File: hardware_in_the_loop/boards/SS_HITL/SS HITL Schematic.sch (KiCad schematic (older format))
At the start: 24 parts, among them J1 CONN_02X03, U2 ATMEGA16M1, Y1 Crystal_SMD

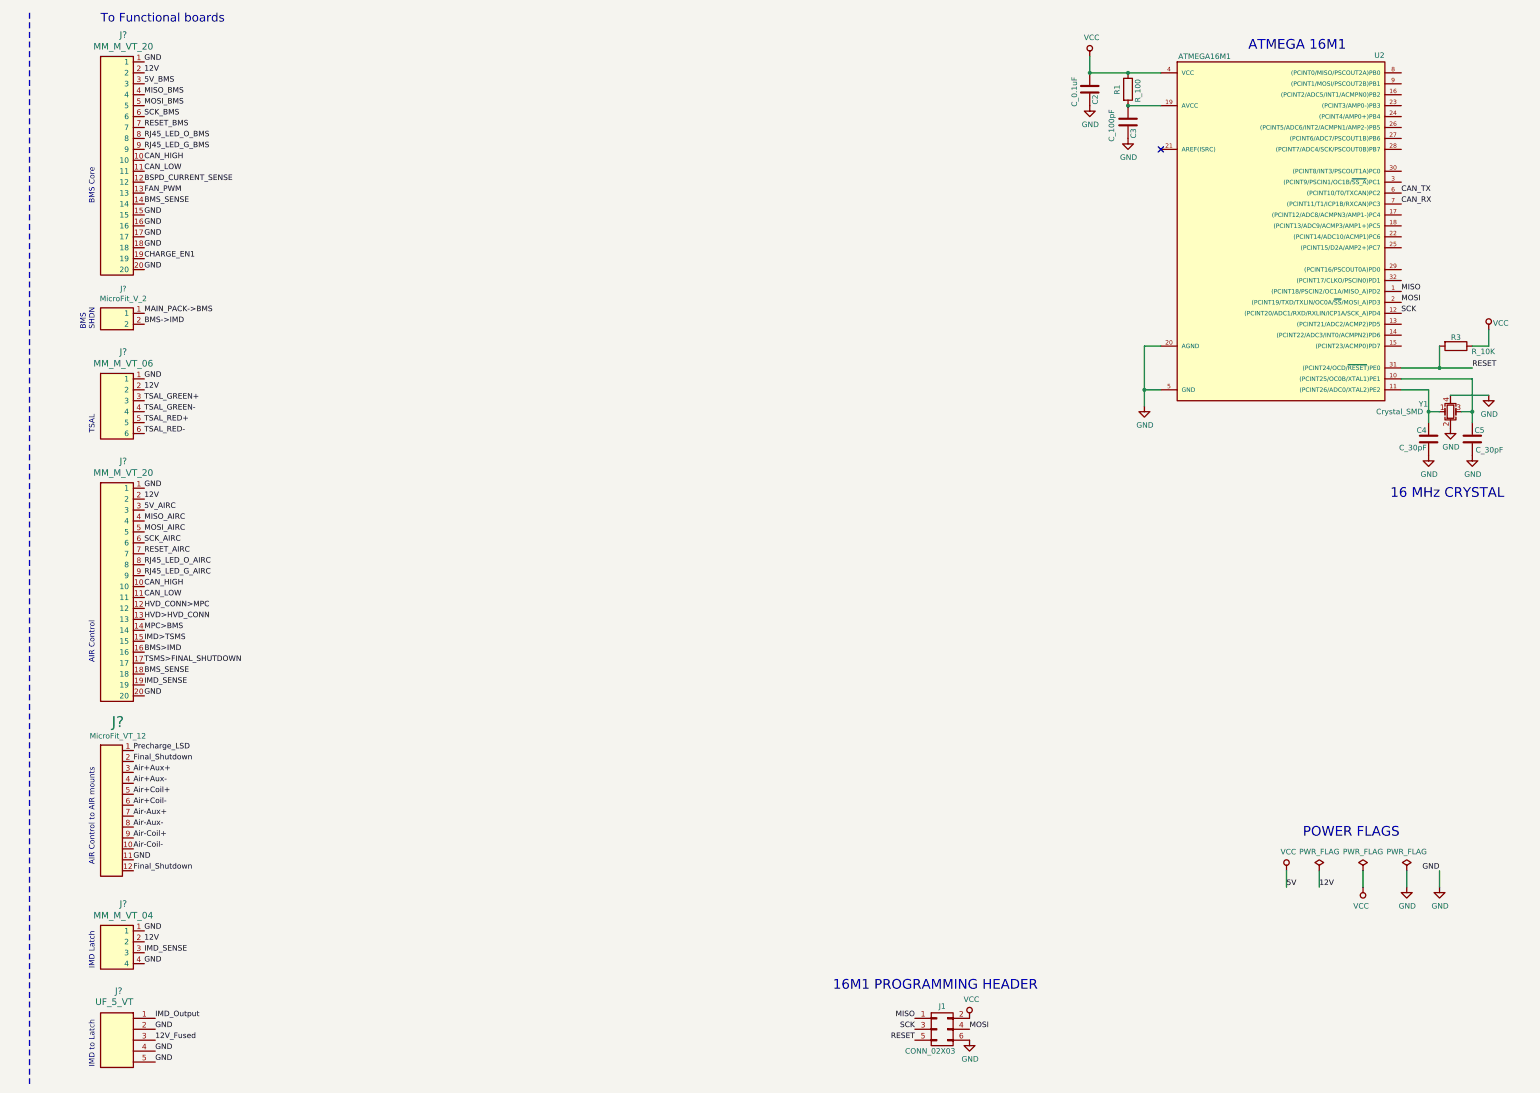
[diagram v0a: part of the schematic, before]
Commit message: Finalized pins on connectors, started to block out mux/demux.
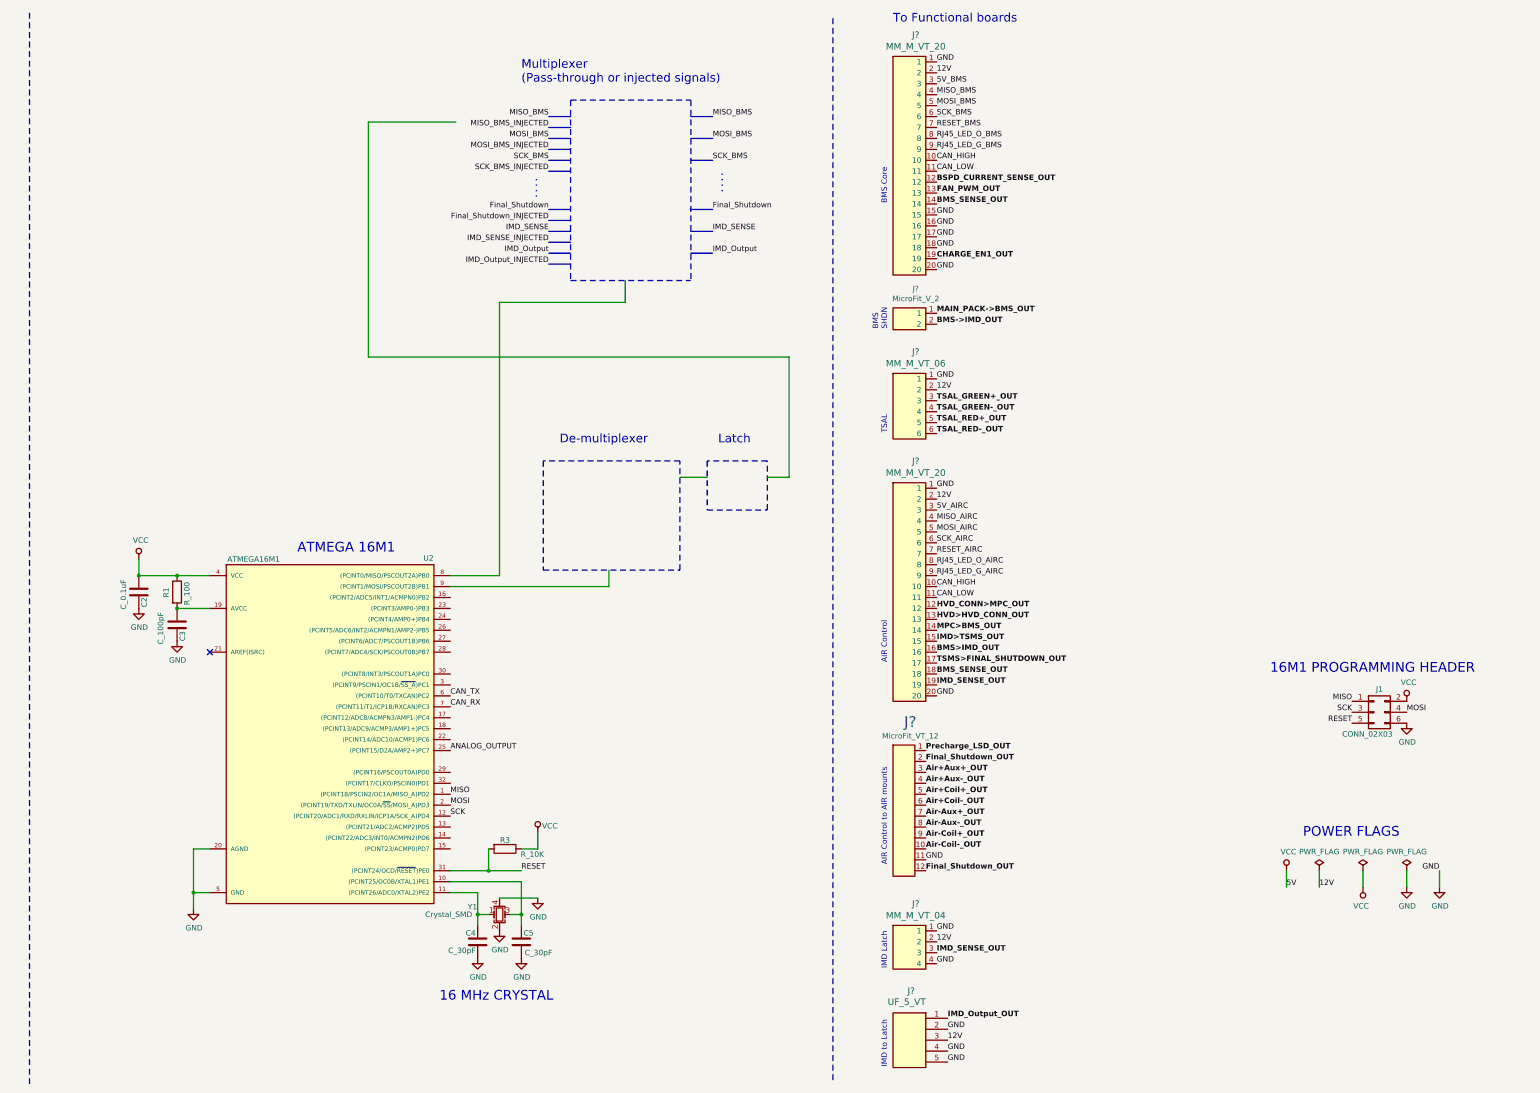
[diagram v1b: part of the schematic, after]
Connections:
- net labels added: ANALOG_OUTPUT, Air+Aux+_OUT, Air+Aux-_OUT, Air+Coil+_OUT, Air+Coil-_OUT, Air-Aux+_OUT, Air-Aux-_OUT, Air-Coil+_OUT, Air-Coil-_OUT, BMS->IMD_OUT, BMS>IMD_OUT, BMS_SENSE_OUT, BSPD_CURRENT_SENSE_OUT, CHARGE_EN1_OUT, FAN_PWM_OUT, Final_Shutdown_INJECTED, Final_Shutdown_OUT, HVD>HVD_CONN_OUT, HVD_CONN>MPC_OUT, IMD>TSMS_OUT, IMD_Output_INJECTED, IMD_Output_OUT, IMD_SENSE_INJECTED, IMD_SENSE_OUT, MAIN_PACK->BMS_OUT, MISO_BMS_INJECTED, MOSI_BMS_INJECTED, MPC>BMS_OUT, Precharge_LSD_OUT, SCK_BMS_INJECTED, TSAL_GREEN+_OUT, TSAL_GREEN-_OUT, TSAL_RED+_OUT, TSAL_RED-_OUT, TSMS>FINAL_SHUTDOWN_OUT
- wire segments 27 -> 39
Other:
- note added: ". . . ."
- note added: "De-multiplexer"
- note added: "Latch"
- note added: "Multiplexer\n(Pass-through or injected signals)"
- moved on the sheet: C2, C3, C4, C5, J1, J?, R1, R3, U2, Y1

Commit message: Completed mux/demux blockout; ready for design review 1
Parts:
- gave numbers to parts that had none: 15
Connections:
- net labels added: BMS_SENSE_OUT_INJECTED, BSPD_CURRENT_SENSE_INJECTED, FAN_PWM_OUT_INJECTED, FINAL_SHUTDOWN, FINAL_SHUTDOWN_INJECTED, FINAL_SHUTDOWN_OUT, IMD_OUTPUT, IMD_OUTPUT_INJECTED, IMD_OUTPUT_OUT, PRECHARGE_LSD, PRECHARGE_LSD_OUT
- net labels removed: 12V_Fused, Final_Shutdown, Final_Shutdown_INJECTED, Final_Shutdown_OUT, IMD_Output, IMD_Output_INJECTED, IMD_Output_OUT, MISO_BMS_INJECTED, MOSI_BMS_INJECTED, Precharge_LSD, Precharge_LSD_OUT, SCK_BMS_INJECTED
- wire segments 39 -> 45
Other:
- note added: ". . ."
- note added: "Bolded labels indicate\noutputs supported by\nHITL injection."
- note added: "De-Multiplexer"
- note added: "Injected signal"
- note added: "Output selectors"
- note added: "Toggle pass-through vs. Inject"
- note removed: ". . . ."
- note removed: "De-multiplexer"
- moved on the sheet: C2, C3, C4, C5, J0, J12, J5, R1, R3, U2, Y1
